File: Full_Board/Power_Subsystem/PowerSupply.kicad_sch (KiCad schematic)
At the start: 22 parts, among them IC4 LM2576HVS-5.0_NOPB, J7 KLDHCX-8-0202-A, U1 LM2576SX-3.3-NOPB

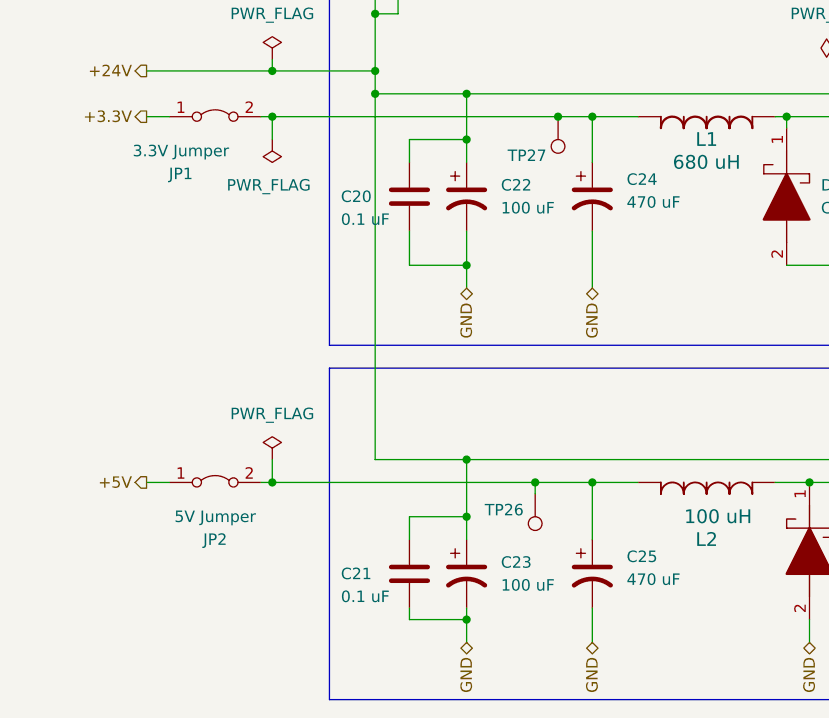
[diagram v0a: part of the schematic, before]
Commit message: Redo sensor network, redo MSP432 connections, redo LED subsystem, add shunts throughout, ERC still passes
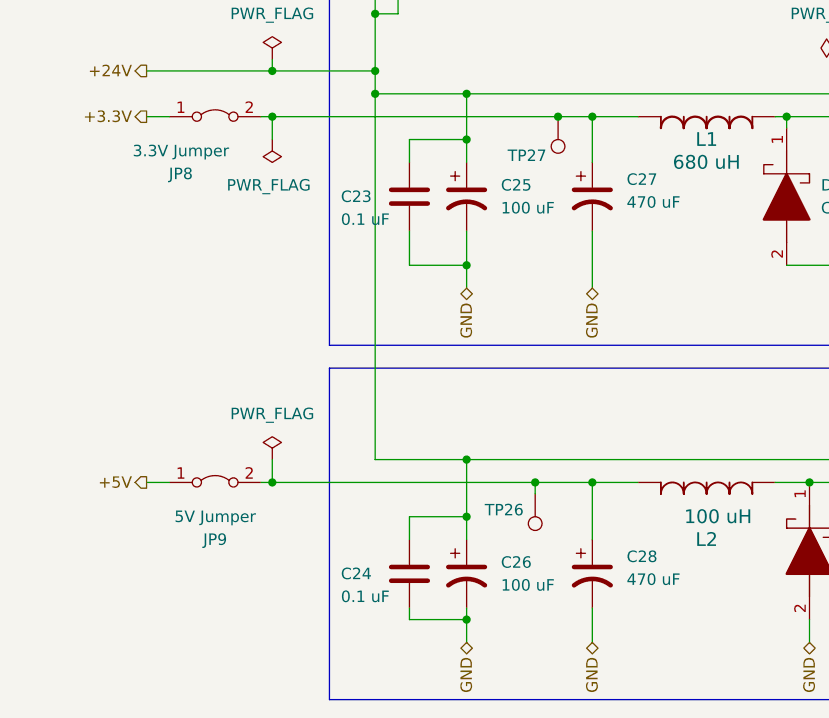
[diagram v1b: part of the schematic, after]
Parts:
- F1: footprint 3588:3588 -> 3588; Manufacturer_Part_Number (none) -> 3588
- renumbered C20 to C23, C21 to C24, C22 to C25, C23 to C26, C24 to C27, C25 to C28, JP1 to JP8, JP2 to JP9
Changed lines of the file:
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@@
   (symbol (lib_id "Device:C_Polarized_US") (at 140.97 146.05 0) (unit 1)
     (in_bom yes) (on_board yes) (fields_autoplaced)
-    (property "Reference" "C25" (id 0) (at 144.78 144.1449 0)
+    (property "Reference" "C28" (id 0) (at 144.78 144.1449 0)
       (effects (font (size 1.27 1.27)) (justify left))
     )
@@
   (symbol (lib_id "power:PWR_FLAG") (at 119.38 43.18 0) (unit 1)
     (in_bom yes) (on_board yes)
-    (property "Reference" "#FLG0102" (id 0) (at 119.38 41.275 0)
+    (property "Reference" "#FLG04" (id 0) (at 119.38 41.275 0)
       (effects (font (size 1.27 1.27)) hide)
     )
@@
   (symbol (lib_id "Device:C_Polarized_US") (at 127 146.05 0) (unit 1)
     (in_bom yes) (on_board yes)
-    (property "Reference" "C23" (id 0) (at 130.81 144.78 0)
+    (property "Reference" "C26" (id 0) (at 130.81 144.78 0)
       (effects (font (size 1.27 1.27)) (justify left))
     )
@@
   (symbol (lib_id "power:PWR_FLAG") (at 105.41 88.9 0) (unit 1)
     (in_bom yes) (on_board yes) (fields_autoplaced)
-    (property "Reference" "#FLG0103" (id 0) (at 105.41 86.995 0)
+    (property "Reference" "#FLG01" (id 0) (at 105.41 86.995 0)
       (effects (font (size 1.27 1.27)) hide)
     )
@@
       (effects (font (size 1.27 1.27)) (justify left))
     )
-    (property "Footprint" "3588:3588" (id 2) (at 121.92 76.2 0)
+    (property "Footprint" "3588" (id 2) (at 121.92 76.2 0)
       (effects (font (size 1.27 1.27)) (justify left) hide)
     )
@@
     (property "Goes With" "https://www.digikey.com/en/products/detail/littelfuse-inc/0297010-WXT/5233693" (id 13) (at 119.38 59.69 90)
       (effects (font (size 1.27 1.27)) hide)
+    )
+    (property "Manufacturer_Part_Number" "3588" (id 14) (at 104.14 76.2 0)
+      (effects (font (size 1.27 1.27)) (justify left) hide)
     )
     (pin "1")
@@
   (symbol (lib_id "Device:C") (at 120.65 146.05 0) (unit 1)
     (in_bom yes) (on_board yes)
-    (property "Reference" "C21" (id 0) (at 113.03 146.05 0)
+    (property "Reference" "C24" (id 0) (at 113.03 146.05 0)
       (effects (font (size 1.27 1.27)) (justify left))
     )
@@
   (symbol (lib_id "Jumper:Jumper_2_Bridged") (at 99.06 135.89 0) (unit 1)
     (in_bom yes) (on_board yes)
-    (property "Reference" "JP2" (id 0) (at 99.06 142.24 0))
+    (property "Reference" "JP9" (id 0) (at 99.06 142.24 0))
     (property "Value" "5V Jumper" (id 1) (at 99.06 139.7 0))
     (property "Footprint" "TestPoint:TestPoint_2Pads_Pitch2.54mm_Drill0.8mm" (id 2) (at 99.06 135.89 0)
       (effects (font (size 1.27 1.27)) hide)
     )
-    (property "Datasheet" "https://app.adam-tech.com/products/download/data_sheet/201605/ph1-xx-ua-data-sheet.pdf" (id 3) (at 99.06 135.89 0)
+    (property "Datasheet" "~" (id 3) (at 99.06 135.89 0)
       (effects (font (size 1.27 1.27)) hide)
     )
@@
   (symbol (lib_id "Jumper:Jumper_2_Bridged") (at 99.06 95.25 0) (unit 1)
     (in_bom yes) (on_board yes)
-    (property "Reference" "JP1" (id 0) (at 95.25 101.6 0))
+    (property "Reference" "JP8" (id 0) (at 95.25 101.6 0))
     (property "Value" "3.3V Jumper" (id 1) (at 95.25 99.06 0))
     (property "Footprint" "TestPoint:TestPoint_2Pads_Pitch2.54mm_Drill0.8mm" (id 2) (at 99.06 95.25 0)
       (effects (font (size 1.27 1.27)) hide)
     )
-    (property "Datasheet" "https://app.adam-tech.com/products/download/data_sheet/201605/ph1-xx-ua-data-sheet.pdf" (id 3) (at 99.06 95.25 0)
+    (property "Datasheet" "~" (id 3) (at 99.06 95.25 0)
       (effects (font (size 1.27 1.27)) hide)
     )
@@
   (symbol (lib_id "Device:C") (at 120.65 104.14 0) (unit 1)
     (in_bom yes) (on_board yes)
-    (property "Reference" "C20" (id 0) (at 113.03 104.14 0)
+    (property "Reference" "C23" (id 0) (at 113.03 104.14 0)
       (effects (font (size 1.27 1.27)) (justify left))
     )
@@
   (symbol (lib_id "Device:C_Polarized_US") (at 127 104.14 0) (unit 1)
     (in_bom yes) (on_board yes)
-    (property "Reference" "C22" (id 0) (at 130.81 102.87 0)
+    (property "Reference" "C25" (id 0) (at 130.81 102.87 0)
       (effects (font (size 1.27 1.27)) (justify left))
     )
@@
   (symbol (lib_id "power:PWR_FLAG") (at 105.41 97.79 180) (unit 1)
     (in_bom yes) (on_board yes)
-    (property "Reference" "#FLG0105" (id 0) (at 105.41 99.695 0)
+    (property "Reference" "#FLG02" (id 0) (at 105.41 99.695 0)
       (effects (font (size 1.27 1.27)) hide)
     )
@@
   (symbol (lib_id "power:PWR_FLAG") (at 168.91 87.63 90) (unit 1)
     (in_bom yes) (on_board yes) (fields_autoplaced)
-    (property "Reference" "#FLG0106" (id 0) (at 167.005 87.63 0)
+    (property "Reference" "#FLG06" (id 0) (at 167.005 87.63 0)
       (effects (font (size 1.27 1.27)) hide)
     )
@@
   (symbol (lib_id "power:PWR_FLAG") (at 105.41 133.35 0) (unit 1)
     (in_bom yes) (on_board yes) (fields_autoplaced)
-    (property "Reference" "#FLG0104" (id 0) (at 105.41 131.445 0)
+    (property "Reference" "#FLG03" (id 0) (at 105.41 131.445 0)
       (effects (font (size 1.27 1.27)) hide)
     )
@@
   (symbol (lib_id "power:PWR_FLAG") (at 129.54 48.26 180) (unit 1)
     (in_bom yes) (on_board yes)
-    (property "Reference" "#FLG0101" (id 0) (at 129.54 50.165 0)
+    (property "Reference" "#FLG05" (id 0) (at 129.54 50.165 0)
       (effects (font (size 1.27 1.27)) hide)
     )
@@
   (symbol (lib_id "Device:C_Polarized_US") (at 140.97 104.14 0) (unit 1)
     (in_bom yes) (on_board yes) (fields_autoplaced)
-    (property "Reference" "C24" (id 0) (at 144.78 102.2349 0)
-      (effects (font (size 1.27 1.27)) (justify left))
-    )
+    (property "Reference" "C27" (id 0) (at 144.78 102.2349 0)
+      (effects (font (size 1.27 1.27)) (justify left))
+    )

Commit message: Added LEDs to the power supply
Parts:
- added D? (x2): EAST2012RA2, EAST2012RA2:EAST2012RA2, symbol EAST2012RA2:EAST2012RA2
- added R?: 150, symbol Device:R
- added R?: 47, symbol Device:R
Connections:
- net GND: now also D?.2, D?.2
- net at C28.1, JP9.2 (B), L2.1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: now also R?.2
- net at C27.1, JP8.2 (B), L1.1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: now also R?.1
- new net: D?.1, R?.2
- new net: D?.1, R?.1
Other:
- moved on the sheet: JP8, JP9

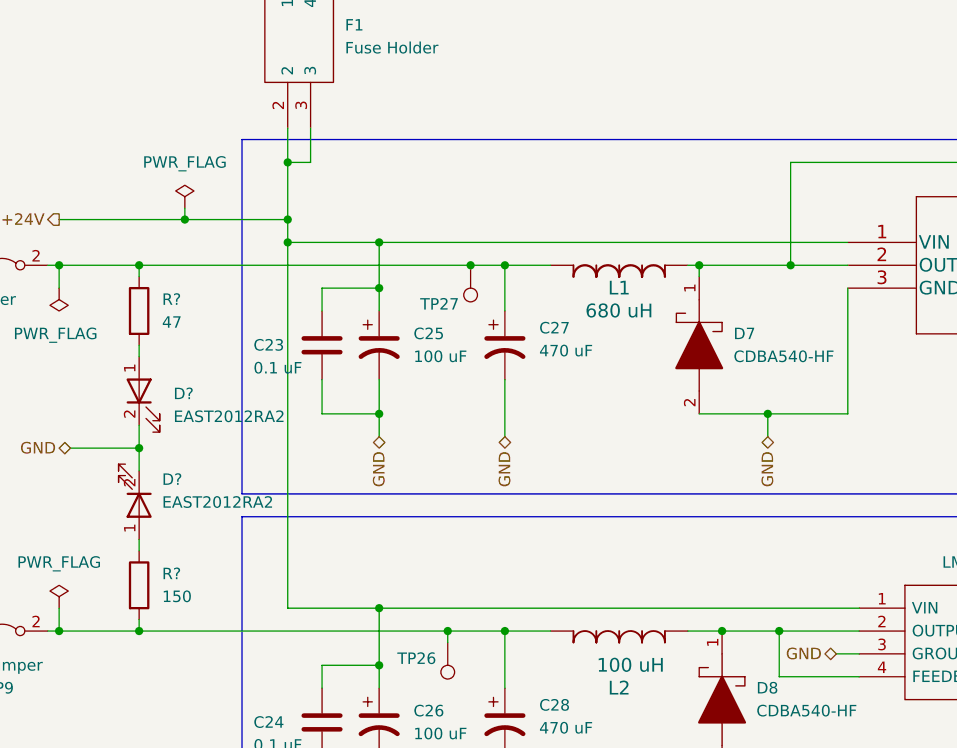
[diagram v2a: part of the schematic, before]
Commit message: Added electromagnet circuit and adjusted the bypass caps
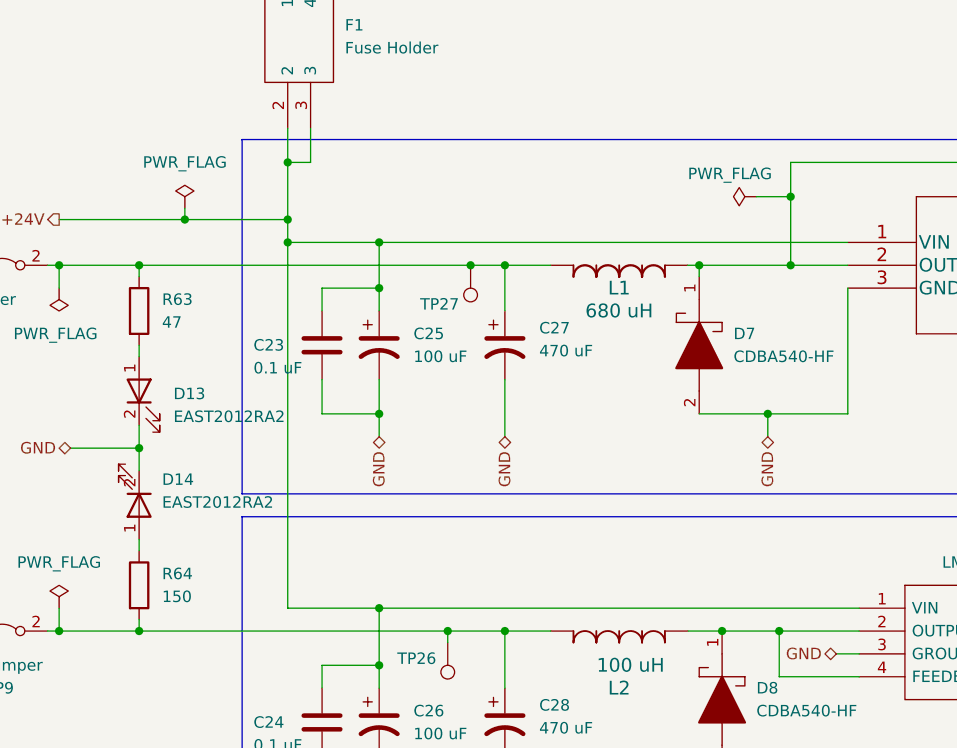
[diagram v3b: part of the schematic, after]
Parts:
- C23, C24: footprint CL05A104KP5NNNC:CL05A104KP5NNNC -> CL10B104KB8NNNC:CL10B104KB8NNNC; Digikey Link https://www.digikey.com/en/products/detail/samsung-electro-mechanics/CL05A104KP5NNNC/3886680 -> https://www.digikey.com/en/products/detail/samsung-electro-mechanics/CL10B104KB8NNNC/3886658; Digikey Part Number 1276-1022-2-ND -> 1276-1000-6-ND; Manufacturers Part Number CL05A104KP5NNNC -> CL10B104KB8NNNC
- gave numbers to parts that had none: 4
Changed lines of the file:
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@@
   (junction (at 224.79 135.89) (diameter 0) (color 0 0 0 0)
+  )
+  (junction (at 172.72 87.63) (diameter 0) (color 0 0 0 0)
   )
   (junction (at 127 46.99) (diameter 0) (color 0 0 0 0)
@@
     (stroke (width 0) (type default) (color 0 0 0 0))
   )
+  (wire (pts (xy 172.72 87.63) (xy 172.72 95.25))
+    (stroke (width 0) (type default) (color 0 0 0 0))
+  )
   (wire (pts (xy 245.11 95.25) (xy 246.38 95.25))
     (stroke (width 0) (type default) (color 0 0 0 0))
@@
     (stroke (width 0) (type default) (color 0 0 0 0))
   )
+  (wire (pts (xy 168.91 87.63) (xy 172.72 87.63))
+    (stroke (width 0) (type default) (color 0 0 0 0))
+  )
   (wire (pts (xy 119.38 46.99) (xy 121.92 46.99))
     (stroke (width 0) (type default) (color 0 0 0 0))
@@
     (stroke (width 0) (type default) (color 0 0 0 0))
   )
-  (wire (pts (xy 172.72 83.82) (xy 172.72 95.25))
+  (wire (pts (xy 172.72 83.82) (xy 172.72 87.63))
     (stroke (width 0) (type default) (color 0 0 0 0))
   )
@@
     )
     (property "Mouser Link" "" (id 8) (at 140.97 146.05 0)
+      (effects (font (size 1.27 1.27)) hide)
+    )
+    (pin "1")
+    (pin "2")
+  )
+  (symbol (lib_id "Device:C") (at 120.65 146.05 0) (unit 1)
+    (in_bom yes) (on_board yes)
+    (property "Reference" "C24" (id 0) (at 113.03 146.05 0)
+      (effects (font (size 1.27 1.27)) (justify left))
+    )
+    (property "Value" "0.1 uF" (id 1) (at 113.03 148.59 0)
+      (effects (font (size 1.27 1.27)) (justify left))
+    )
+    (property "Footprint" "CL10B104KB8NNNC:CL10B104KB8NNNC" (id 2) (at 121.6152 149.86 0)
+      (effects (font (size 1.27 1.27)) hide)
+    )
+    (property "Datasheet" "https://media.digikey.com/pdf/Data%20Sheets/Samsung%20PDFs/CL10B104KB8NNNC_Spec.pdf" (id 3) (at 120.65 146.05 0)
+      (effects (font (size 1.27 1.27)) hide)
+    )
+    (property "Manufacturers Part Number" "CL10B104KB8NNNC" (id 4) (at 120.65 146.05 0)
+      (effects (font (size 1.27 1.27)) hide)
+    )
+    (property "Digikey Part Number" "1276-1000-6-ND" (id 5) (at 120.65 146.05 0)
+      (effects (font (size 1.27 1.27)) hide)
+    )
+    (property "Mouser Part Number" "" (id 6) (at 120.65 146.05 0)
+      (effects (font (size 1.27 1.27)) hide)
+    )
+    (property "Digikey Link" "https://www.digikey.com/en/products/detail/samsung-electro-mechanics/CL10B104KB8NNNC/3886658" (id 7) (at 120.65 146.05 0)
+      (effects (font (size 1.27 1.27)) hide)
+    )
+    (property "Mouser Link" "" (id 8) (at 120.65 146.05 0)
       (effects (font (size 1.27 1.27)) hide)
     )
@@
   (symbol (lib_id "EAST2012RA2:EAST2012RA2") (at 100.33 109.22 90) (unit 1)
     (in_bom yes) (on_board yes) (fields_autoplaced)
-    (property "Reference" "D?" (id 0) (at 104.14 109.5374 90)
+    (property "Reference" "D13" (id 0) (at 104.14 109.5374 90)
       (effects (font (size 1.27 1.27)) (justify right))
     )
@@
   (symbol (lib_id "EAST2012RA2:EAST2012RA2") (at 100.33 121.92 270) (unit 1)
     (in_bom yes) (on_board yes) (fields_autoplaced)
-    (property "Reference" "D?" (id 0) (at 102.87 119.0624 90)
+    (property "Reference" "D14" (id 0) (at 102.87 119.0624 90)
       (effects (font (size 1.27 1.27)) (justify left))
     )
@@
     )
     (property "Mouser Link" "" (id 8) (at 100.33 121.92 0)
-      (effects (font (size 1.27 1.27)) hide)
-    )
-    (pin "1")
-    (pin "2")
-  )
-  (symbol (lib_id "Device:C") (at 120.65 146.05 0) (unit 1)
-    (in_bom yes) (on_board yes)
-    (property "Reference" "C24" (id 0) (at 113.03 146.05 0)
-      (effects (font (size 1.27 1.27)) (justify left))
-    )
-    (property "Value" "0.1 uF" (id 1) (at 113.03 148.59 0)
-      (effects (font (size 1.27 1.27)) (justify left))
-    )
-    (property "Footprint" "CL05A104KP5NNNC:CL05A104KP5NNNC" (id 2) (at 121.6152 149.86 0)
-      (effects (font (size 1.27 1.27)) hide)
-    )
-    (property "Datasheet" "~" (id 3) (at 120.65 146.05 0)
-      (effects (font (size 1.27 1.27)) hide)
-    )
-    (property "Manufacturers Part Number" "CL05A104KP5NNNC" (id 4) (at 120.65 146.05 0)
-      (effects (font (size 1.27 1.27)) hide)
-    )
-    (property "Digikey Part Number" "1276-1022-2-ND" (id 5) (at 120.65 146.05 0)
-      (effects (font (size 1.27 1.27)) hide)
-    )
-    (property "Mouser Part Number" "" (id 6) (at 120.65 146.05 0)
-      (effects (font (size 1.27 1.27)) hide)
-    )
-    (property "Digikey Link" "https://www.digikey.com/en/products/detail/samsung-electro-mechanics/CL05A104KP5NNNC/3886680" (id 7) (at 120.65 146.05 0)
-      (effects (font (size 1.27 1.27)) hide)
-    )
-    (property "Mouser Link" "" (id 8) (at 120.65 146.05 0)
       (effects (font (size 1.27 1.27)) hide)
     )
@@
       (effects (font (size 1.27 1.27)) (justify left))
     )
-    (property "Footprint" "CL05A104KP5NNNC:CL05A104KP5NNNC" (id 2) (at 121.6152 107.95 0)
-      (effects (font (size 1.27 1.27)) hide)
-    )
-    (property "Datasheet" "~" (id 3) (at 120.65 104.14 0)
-      (effects (font (size 1.27 1.27)) hide)
-    )
-    (property "Manufacturers Part Number" "CL05A104KP5NNNC" (id 4) (at 120.65 104.14 0)
-      (effects (font (size 1.27 1.27)) hide)
-    )
-    (property "Digikey Part Number" "1276-1022-2-ND" (id 5) (at 120.65 104.14 0)
+    (property "Footprint" "CL10B104KB8NNNC:CL10B104KB8NNNC" (id 2) (at 121.6152 107.95 0)
+      (effects (font (size 1.27 1.27)) hide)
+    )
+    (property "Datasheet" "https://media.digikey.com/pdf/Data%20Sheets/Samsung%20PDFs/CL10B104KB8NNNC_Spec.pdf" (id 3) (at 120.65 104.14 0)
+      (effects (font (size 1.27 1.27)) hide)
+    )
+    (property "Manufacturers Part Number" "CL10B104KB8NNNC" (id 4) (at 120.65 104.14 0)
+      (effects (font (size 1.27 1.27)) hide)
+    )
+    (property "Digikey Part Number" "1276-1000-6-ND" (id 5) (at 120.65 104.14 0)
       (effects (font (size 1.27 1.27)) hide)
     )
@@
       (effects (font (size 1.27 1.27)) hide)
     )
-    (property "Digikey Link" "https://www.digikey.com/en/products/detail/samsung-electro-mechanics/CL05A104KP5NNNC/3886680" (id 7) (at 120.65 104.14 0)
+    (property "Digikey Link" "https://www.digikey.com/en/products/detail/samsung-electro-mechanics/CL10B104KB8NNNC/3886658" (id 7) (at 120.65 104.14 0)
       (effects (font (size 1.27 1.27)) hide)
     )
@@
   (symbol (lib_id "Device:R") (at 100.33 130.81 0) (unit 1)
     (in_bom yes) (on_board yes) (fields_autoplaced)
-    (property "Reference" "R?" (id 0) (at 102.87 129.5399 0)
+    (property "Reference" "R64" (id 0) (at 102.87 129.5399 0)
       (effects (font (size 1.27 1.27)) (justify left))
     )
@@
     (pin "6")
   )
+  (symbol (lib_id "power:PWR_FLAG") (at 168.91 87.63 90) (unit 1)
+    (in_bom yes) (on_board yes)
+    (property "Reference" "#FLG0101" (id 0) (at 167.005 87.63 0)
+      (effects (font (size 1.27 1.27)) hide)
+    )
+    (property "Value" "PWR_FLAG" (id 1) (at 161.29 85.09 90)
+      (effects (font (size 1.27 1.27)) (justify right))
+    )
+    (property "Footprint" "" (id 2) (at 168.91 87.63 0)
+      (effects (font (size 1.27 1.27)) hide)
+    )
+    (property "Datasheet" "~" (id 3) (at 168.91 87.63 0)
+      (effects (font (size 1.27 1.27)) hide)
+    )
+    (pin "1")
+  )
   (symbol (lib_id "Device:C_Polarized_US") (at 140.97 104.14 0) (unit 1)
     (in_bom yes) (on_board yes) (fields_autoplaced)
@@
   (symbol (lib_id "Device:R") (at 100.33 100.33 0) (unit 1)
     (in_bom yes) (on_board yes) (fields_autoplaced)
-    (property "Reference" "R?" (id 0) (at 102.87 99.0599 0)
-      (effects (font (size 1.27 1.27)) (justify left))
-    )
+    (property "Reference" "R63" (id 0) (at 102.87 99.0599 0)
+      (effects (font (size 1.27 1.27)) (justify left))
+    )
